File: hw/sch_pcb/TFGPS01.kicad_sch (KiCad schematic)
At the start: 75 parts, among them J1 SM10B-GHS-TB, J2 USBC_USB4105-GF-A, J3 SM06B-GHS-TB, J4 SM04B-GHS-TB, J5 SM08B-GHS-TB, M1 HOLE, M2 HOLE, M3 HOLE, M4 HOLE, Q1 BC817-25, Q2 BC817-25, Q3 BC817-25, U1 MIC5504-3.3YM5, U2 USBLC6-2SC6, U3 NEO-M8P, U4 MAX2655

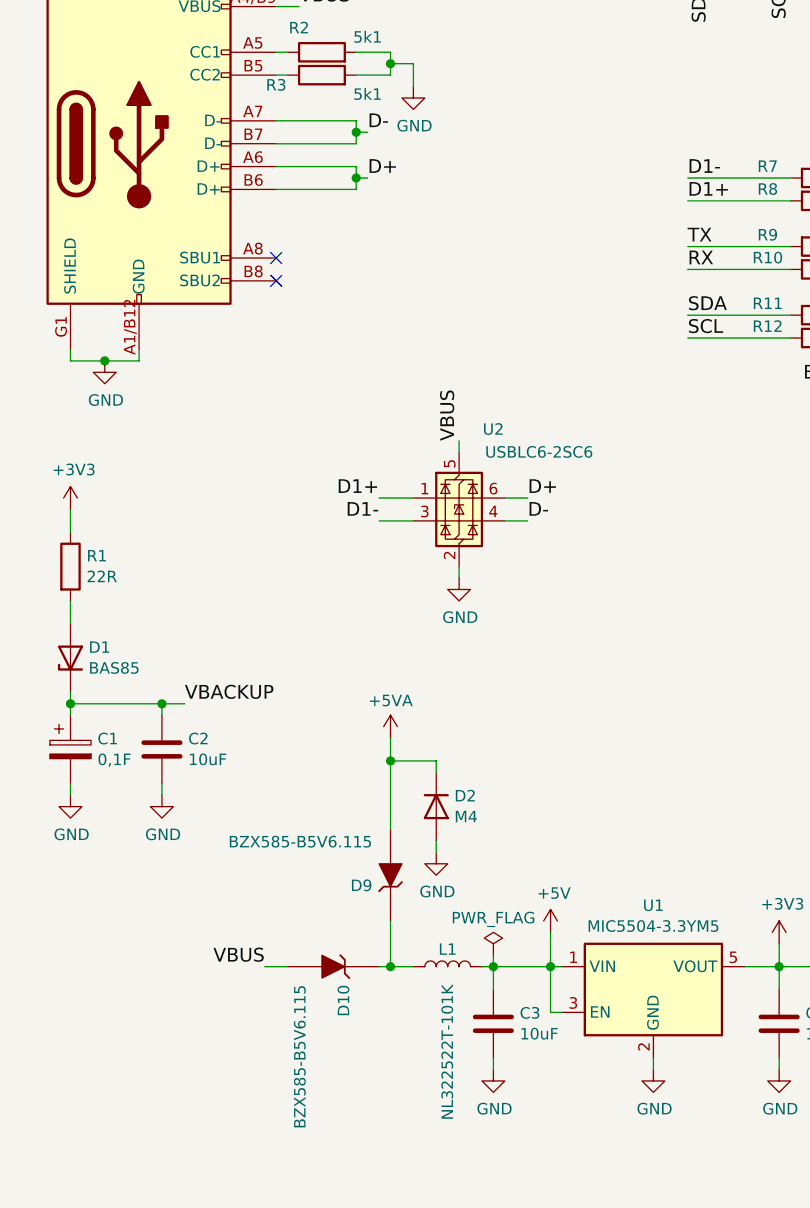
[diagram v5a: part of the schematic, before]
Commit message: Update diode types.
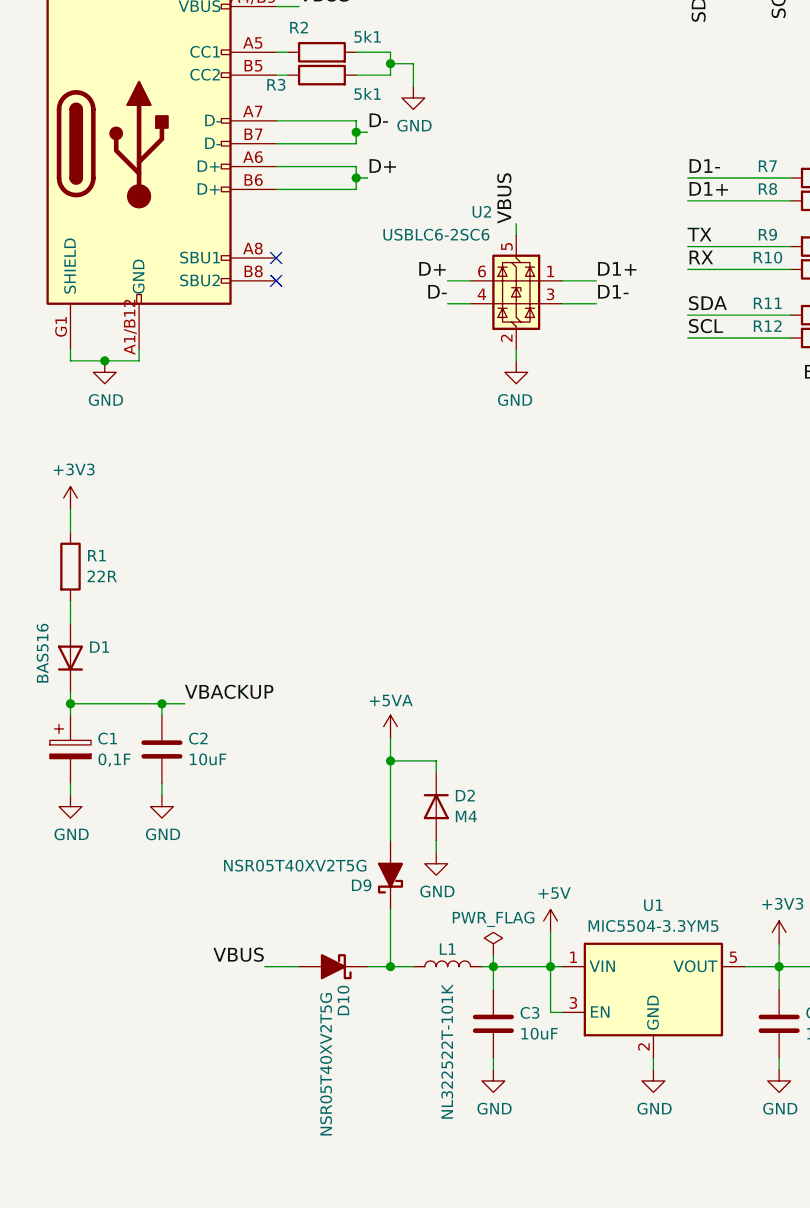
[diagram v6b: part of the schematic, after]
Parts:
- D1: value BAS85 -> BAS516; footprint Diode_SMD:D_MiniMELF -> Diode_SMD:D_SOD-523; symbol Device:D_Zener -> Diode:BAS516
- D10, D9: value BZX585-B5V6.115 -> NSR05T40XV2T5G; symbol MLAB_D:D_ZENER -> Device:D_Schottky_Filled; UST_ID 60879d38128750769ee58e48 -> 5c70984712875079b91f8b7b
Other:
- moved on the sheet: U2
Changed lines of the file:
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@@
 	(wire
 		(pts
+			(xy 52.07 171.45) (xy 54.61 171.45)
+		)
+		(stroke
+			(width 0)
+			(type solid)
+		)
+	)
+	(wire
+		(pts
 			(xy 19.05 151.13) (xy 19.05 152.4)
 		)
@@
 	(wire
 		(pts
-			(xy 67.31 119.38) (xy 69.85 119.38)
+			(xy 63.5 95.25) (xy 60.96 95.25)
 		)
 		(stroke
@@
 	(wire
 		(pts
-			(xy 40.64 171.45) (xy 43.18 171.45)
+			(xy 40.64 171.45) (xy 44.45 171.45)
 		)
 		(stroke
@@
 	(wire
 		(pts
-			(xy 53.34 171.45) (xy 54.61 171.45)
-		)
-		(stroke
-			(width 0)
-			(type solid)
-		)
-	)
-	(wire
-		(pts
 			(xy 133.35 33.02) (xy 135.89 33.02)
 		)
@@
 	(wire
 		(pts
-			(xy 62.23 113.03) (xy 62.23 114.3)
+			(xy 68.58 88.9) (xy 68.58 90.17)
 		)
 		(stroke
@@
 	(wire
 		(pts
-			(xy 53.34 119.38) (xy 57.15 119.38)
+			(xy 77.47 95.25) (xy 73.66 95.25)
 		)
 		(stroke
@@
 	(wire
 		(pts
-			(xy 67.31 121.92) (xy 69.85 121.92)
+			(xy 63.5 97.79) (xy 60.96 97.79)
 		)
 		(stroke
@@
 	(wire
 		(pts
-			(xy 62.23 127) (xy 62.23 128.27)
+			(xy 68.58 102.87) (xy 68.58 104.14)
 		)
 		(stroke
@@
 	(wire
 		(pts
-			(xy 54.61 166.37) (xy 54.61 171.45)
+			(xy 54.61 165.1) (xy 54.61 171.45)
 		)
 		(stroke
@@
 	(wire
 		(pts
-			(xy 57.15 121.92) (xy 53.34 121.92)
+			(xy 73.66 97.79) (xy 77.47 97.79)
 		)
 		(stroke
@@
 	(wire
 		(pts
-			(xy 54.61 148.59) (xy 54.61 156.21)
+			(xy 54.61 148.59) (xy 54.61 157.48)
 		)
 		(stroke
@@
 	)
 	(label "D1-"
-		(at 53.34 121.92 180)
+		(at 77.47 97.79 0)
 		(effects
 			(font
 				(size 1.524 1.524)
 			)
-			(justify right bottom)
+			(justify left bottom)
 		)
 	)
 	(label "D-"
-		(at 69.85 121.92 0)
+		(at 60.96 97.79 180)
 		(effects
 			(font
 				(size 1.524 1.524)
 			)
-			(justify left bottom)
+			(justify right bottom)
 		)
 	)
@@
 	)
 	(label "VBUS"
-		(at 62.23 113.03 90)
+		(at 68.58 88.9 90)
 		(effects
 			(font
@@
 	)
 	(label "D1+"
-		(at 53.34 119.38 180)
+		(at 77.47 95.25 0)
 		(effects
 			(font
 				(size 1.524 1.524)
 			)
-			(justify right bottom)
+			(justify left bottom)
 		)
 	)
@@
 	)
 	(label "D+"
-		(at 69.85 119.38 0)
+		(at 60.96 95.25 180)
 		(effects
 			(font
 				(size 1.524 1.524)
 			)
-			(justify left bottom)
+			(justify right bottom)
 		)
 	)
@@
 	(symbol
 		(lib_id "Power_Protection:USBLC6-2SC6")
-		(at 62.23 119.38 0)
+		(at 68.58 95.25 0)
+		(mirror y)
 		(unit 1)
 		(exclude_from_sim no)
@@
 		(dnp no)
 		(property "Reference" "U2"
-			(at 66.04 111.76 0)
+			(at 64.77 87.63 0)
 			(effects
 				(font
@@
 		)
 		(property "Value" "USBLC6-2SC6"
-			(at 71.12 114.3 0)
+			(at 59.69 90.17 0)
 			(effects
 				(font
@@
 		)
 		(property "Footprint" "Package_TO_SOT_SMD:SOT-23-6"
-			(at 43.18 109.22 0)
+			(at 87.63 85.09 0)
 			(effects
 				(font
@@
 		)
 		(property "Datasheet" "http://www2.st.com/resource/en/datasheet/CD00050750.pdf"
-			(at 67.31 110.49 0)
+			(at 63.5 86.36 0)
 			(effects
 				(font
@@
 		)
 		(property "Description" ""
-			(at 62.23 119.38 0)
+			(at 68.58 95.25 0)
 			(effects
 				(font
@@
 		)
 		(property "UST_ID" "5e82e0691287502a334a778c"
-			(at 62.23 104.4194 0)
+			(at 68.58 80.2894 0)
 			(effects
 				(font
@@
 	)
 	(symbol
-		(lib_id "Device:D_Zener")
+		(lib_id "Diode:BAS516")
 		(at 19.05 137.16 90)
 		(unit 1)
@@
 			)
 		)
-		(property "Value" "BAS85"
-			(at 21.0566 138.303 90)
+		(property "Value" "BAS516"
+			(at 16.002 136.652 0)
 			(effects
 				(font
 					(size 1.27 1.27)
 				)
-				(justify right)
 			)
 		)
-		(property "Footprint" "Diode_SMD:D_MiniMELF"
-			(at 19.05 137.16 0)
+		(property "Footprint" "Diode_SMD:D_SOD-523"
+			(at 23.495 137.16 0)
 			(effects
 				(font
@@
 			)
 		)
-		(property "Datasheet" "~"
+		(property "Datasheet" "https://assets.nexperia.com/documents/data-sheet/BAS16_SER.pdf"
 			(at 19.05 137.16 0)
 			(effects
@@
 			)
 		)
-		(property "Description" ""
+		(property "Description" "100V, 0.25A, High-speed Switching Diode, SOD-523"
 			(at 19.05 137.16 0)
 			(effects
@@
 					(size 1.27 1.27)
 				)
+				(hide yes)
 			)
 		)
@@
 			)
 		)
+		(property "Sim.Device" "D"
+			(at 19.05 137.16 0)
+			(effects
+				(font
+					(size 1.27 1.27)
+				)
+				(hide yes)
+			)
+		)
+		(property "Sim.Pins" "1=K 2=A"
+			(at 19.05 137.16 0)
+			(effects
+				(font
+					(size 1.27 1.27)
+				)
+				(hide yes)
+			)
+		)
 		(pin "1"
 		)
@@
 	(symbol
 		(lib_id "power:GND")
-		(at 62.23 128.27 0)
+		(at 68.58 104.14 0)
+		(mirror y)
 		(unit 1)
 		(exclude_from_sim no)
@@
 		(dnp no)
 		(property "Reference" "#PWR012"
-			(at 62.23 134.62 0)
+			(at 68.58 110.49 0)
 			(effects
 				(font
@@
 		)
 		(property "Value" "GND"
-			(at 62.357 132.6642 0)
+			(at 68.453 108.5342 0)
 			(effects
 				(font
@@
 		)
 		(property "Footprint" ""
-			(at 62.23 128.27 0)
+			(at 68.58 104.14 0)
 			(effects
 				(font
@@
 		)
 		(property "Datasheet" ""
-			(at 62.23 128.27 0)
+			(at 68.58 104.14 0)
 			(effects
 				(font
@@
 		)
 		(property "Description" ""
-			(at 62.23 128.27 0)
+			(at 68.58 104.14 0)
 			(effects
 				(font
@@
 	)
 	(symbol
-		(lib_id "MLAB_D:D_ZENER")
+		(lib_id "Device:D_Schottky_Filled")
 		(at 48.26 171.45 180)
 		(unit 1)
@@
 			)
 		)
-		(property "Value" "BZX585-B5V6.115"
-			(at 44.577 173.457 90)
+		(property "Value" "NSR05T40XV2T5G"
+			(at 47.498 174.244 90)
 			(effects
 				(font
@@
 			)
 		)
-		(property "UST_id" ""
-			(at 48.26 171.45 0)
-			(effects
-				(font
-					(size 1.27 1.27)
-				)
-				(hide yes)
-			)
-		)
-		(property "UST_ID" "60879d38128750769ee58e48"
+		(property "UST_ID" "5c70984712875079b91f8b7b"
 			(at 48.26 171.45 0)
 			(effects
@@
 	)
 	(symbol
-		(lib_id "MLAB_D:D_ZENER")
+		(lib_id "Device:D_Schottky_Filled")
 		(at 54.61 161.29 90)
 		(unit 1)
@@
 			)
 		)
-		(property "Value" "BZX585-B5V6.115"
-			(at 52.603 157.607 90)
+		(property "Value" "NSR05T40XV2T5G"
+			(at 52.07 160.274 90)
 			(effects
 				(font
@@
 			)
 		)
-		(property "UST_id" ""
-			(at 54.61 161.29 0)
-			(effects
-				(font
-					(size 1.27 1.27)
-				)
-				(hide yes)
-			)
-		)
-		(property "UST_ID" "60879d38128750769ee58e48"
+		(property "UST_ID" "5c70984712875079b91f8b7b"
 			(at 54.61 161.29 0)
 			(effects

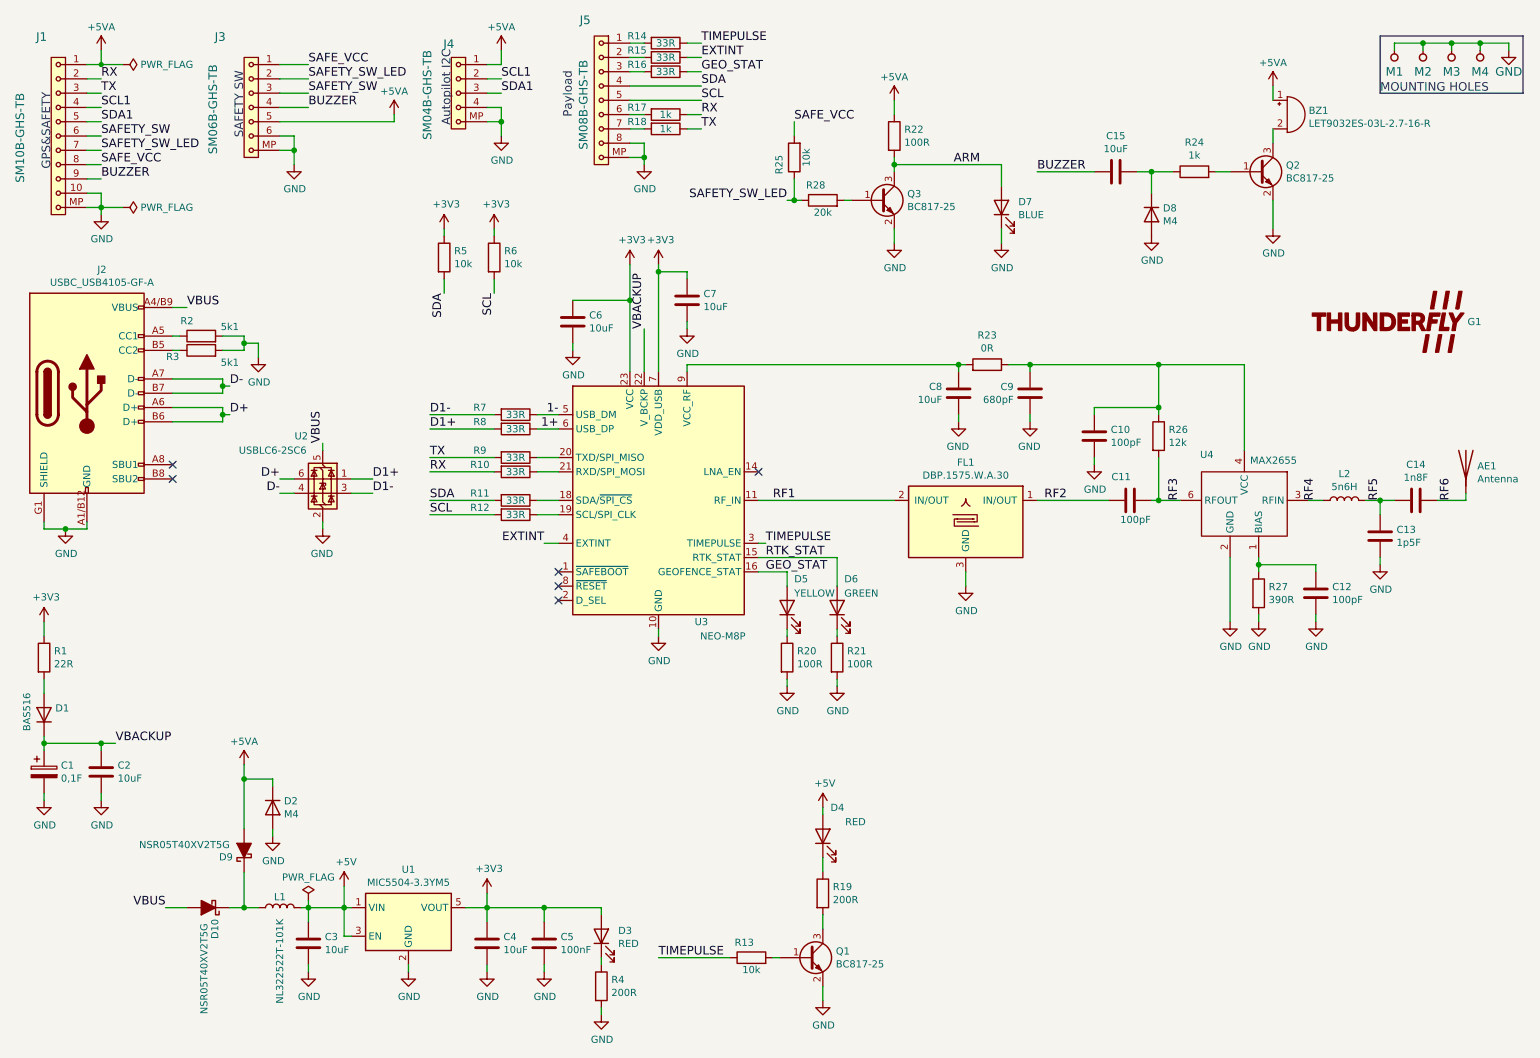
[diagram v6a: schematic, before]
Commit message: Improve layout and LED footprints.
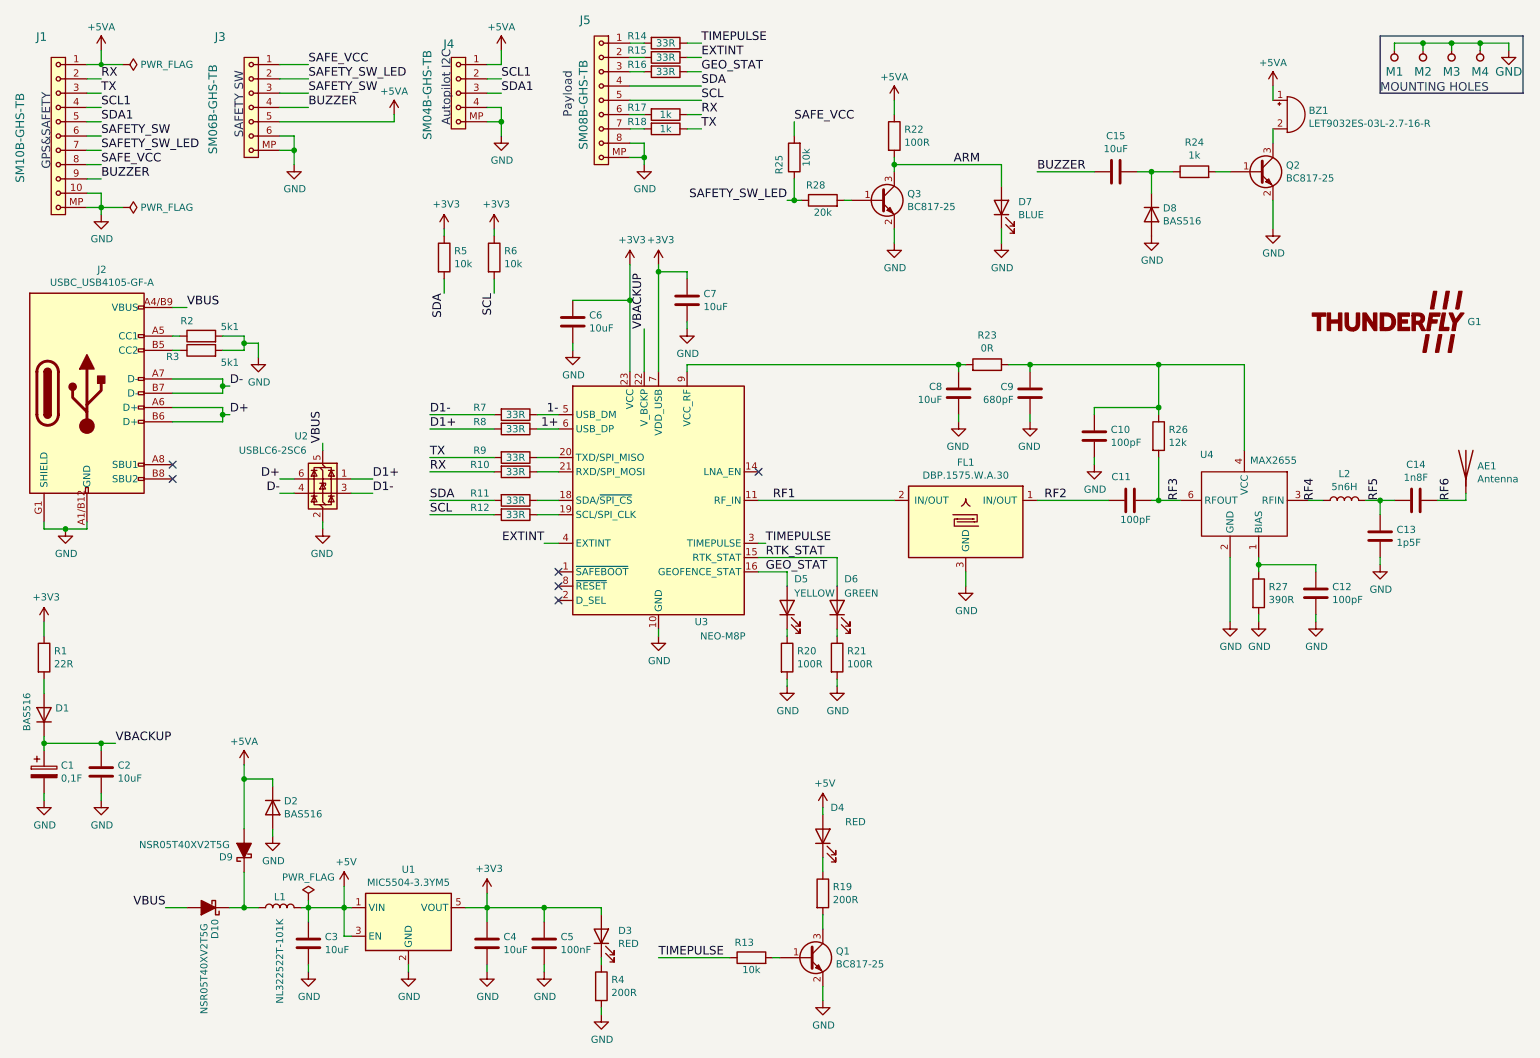
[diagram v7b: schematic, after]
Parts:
- D1: UST_ID 5c70984512875079b91f88b3 -> 693421c6ea235ce78ba25972
- D2, D8: value M4 -> BAS516; footprint Diode_SMD:D_SMA -> Diode_SMD:D_SOD-523; UST_ID 5c70984512875079b91f88ac -> 693421c6ea235ce78ba25972
- D3, D4, D5, D6, D7: footprint Mlab_D:LED_1206 -> Mlab_D:LED_1206_mill
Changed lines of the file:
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@@
 			)
 		)
-		(property "UST_ID" "5c70984512875079b91f88b3"
+		(property "UST_ID" "693421c6ea235ce78ba25972"
 			(at 19.05 137.16 0)
 			(effects
@@
 			)
 		)
-		(property "Footprint" "Mlab_D:LED_1206"
+		(property "Footprint" "Mlab_D:LED_1206_mill"
 			(at 118.11 176.53 0)
 			(effects
@@
 			)
 		)
-		(property "Value" "M4"
+		(property "Value" "BAS516"
 			(at 61.6966 154.813 90)
 			(effects
@@
 			)
 		)
-		(property "Footprint" "Diode_SMD:D_SMA"
+		(property "Footprint" "Diode_SMD:D_SOD-523"
 			(at 59.69 153.67 0)
 			(effects
@@
 			)
 		)
-		(property "UST_ID" "5c70984512875079b91f88ac"
+		(property "UST_ID" "693421c6ea235ce78ba25972"
 			(at 59.69 153.67 0)
 			(effects
@@
 			)
 		)
-		(property "Footprint" "Mlab_D:LED_1206"
+		(property "Footprint" "Mlab_D:LED_1206_mill"
 			(at 151.13 118.11 0)
 			(effects
@@
 			)
 		)
-		(property "Footprint" "Mlab_D:LED_1206"
+		(property "Footprint" "Mlab_D:LED_1206_mill"
 			(at 160.02 118.11 0)
 			(effects
@@
 			)
 		)
-		(property "Footprint" "Mlab_D:LED_1206"
+		(property "Footprint" "Mlab_D:LED_1206_mill"
 			(at 157.48 158.75 0)
 			(effects
@@
 			)
 		)
-		(property "Footprint" "Mlab_D:LED_1206"
+		(property "Footprint" "Mlab_D:LED_1206_mill"
 			(at 189.23 46.99 0)
 			(effects
@@
 			)
 		)
-		(property "Value" "M4"
+		(property "Value" "BAS516"
 			(at 217.9321 49.4093 90)
 			(effects
@@
 			)
 		)
-		(property "Footprint" "Diode_SMD:D_SMA"
+		(property "Footprint" "Diode_SMD:D_SOD-523"
 			(at 215.9 48.26 0)
 			(effects
@@
 			)
 		)
-		(property "UST_ID" "5c70984512875079b91f88ac"
+		(property "UST_ID" "693421c6ea235ce78ba25972"
 			(at 215.9 48.26 0)
 			(effects
